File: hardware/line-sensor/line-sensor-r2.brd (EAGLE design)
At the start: 112 x 60 mm, 107 parts, among them IC1 GP2S60, IC10 GP2S60, IC11 GP2S60, IC12 GP2S60, IC13 GP2S60, IC14 GP2S60, IC15 GP2S60, IC16 GP2S60, IC17 GP2S60, IC18 GP2S60, IC19 GP2S60, IC2 GP2S60, IC20 GP2S60, IC21 GP2S60, IC22 GP2S60, IC23 GP2S60, IC24 STM32L151VE, IC25 GP2S60, IC26 GP2S60, IC27 ADR366BUJZ, IC28 TI-TPS62170, IC29 TI-LM5165YDRCR, IC3 GP2S60, IC30 ADP124ARHZ-3.3-R7CT-ND, IC4 GP2S60, IC5 GP2S60, IC6 GP2S60, IC7 GP2S60, IC8 GP2S60, IC9 GP2S60

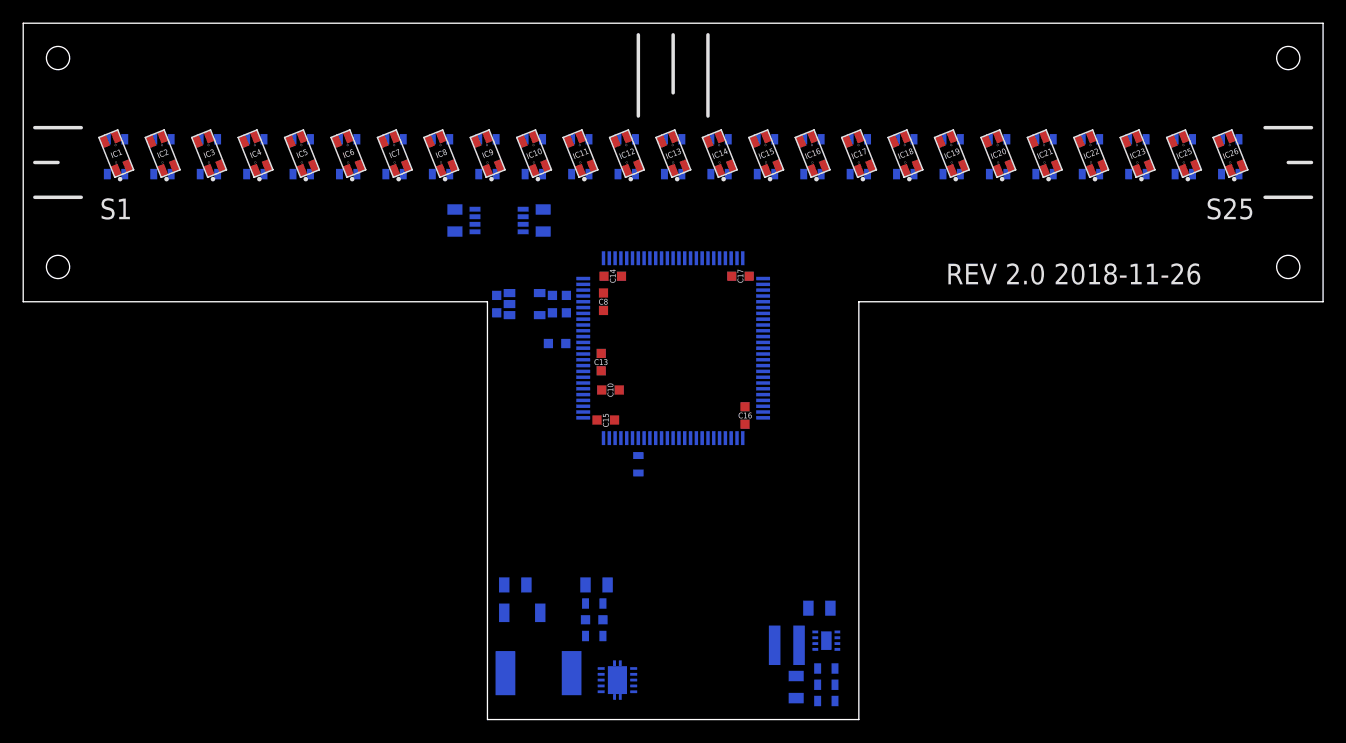
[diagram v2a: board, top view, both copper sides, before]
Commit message: - added line sensor power layout and mcu pin usage configuration
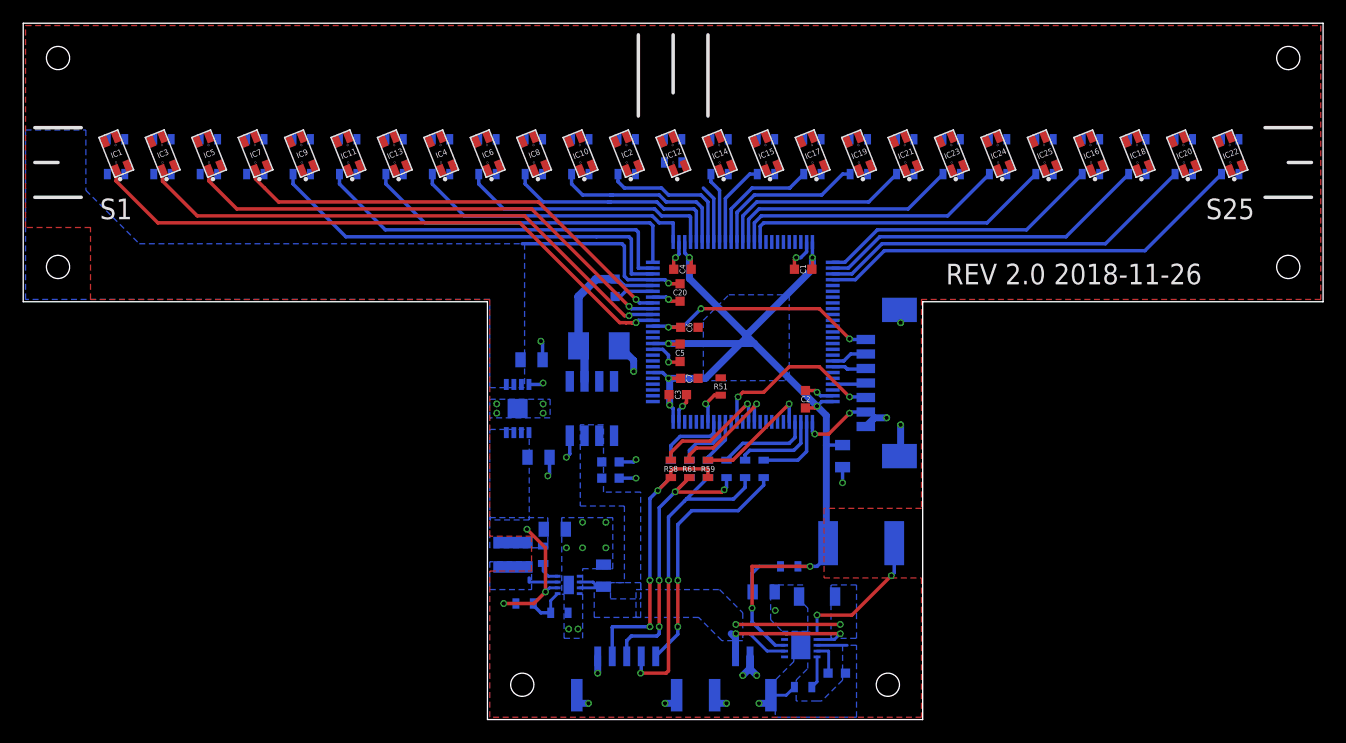
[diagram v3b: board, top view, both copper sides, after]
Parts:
- added C20: 0.1u 10V X7R, capacitors:CAPACITOR-0603
- added J1: MOLEX-502382-02XX, connectors:MOLEX-502382-02XX
- added J2: MOLEX-502382-05XX, connectors:MOLEX-502382-05XX
- added J3: MOLEX-53261-0771, connectors:MOLEX-53261-0771
- added R57, R58, R59, R60, R61, R62, R63, R64, R65: 0, resistors:RESISTOR-0603
- C1: value 0.1u 10V -> 0.1u
- C10: value 0.1u -> 33n 10V X7R
- C11: value 33n 10V X7R -> 22u 10V X7S; device capacitors:CAPACITOR-0603 -> capacitors:CAPACITOR-0805
- C13: value 0.1u -> 22u 10V X7R; device capacitors:CAPACITOR-0603 -> capacitors:CAPACITOR-0805
- C14: value 0.1u -> 10u 50V
- C15, C18: value 0.1u -> 1u 10V X7R; device capacitors:CAPACITOR-0603 -> capacitors:CAPACITOR-0805
- C16: value 0.1u -> 0.1u 50V
- C17: value 0.1u -> 1u 10V Tant; device capacitors:CAPACITOR-0603 -> capacitors:CAPACITOR_POLARIZED-1411-(3528-MET)
- C19: value 22u 10V X7R -> 0.1u 10V X7R; device capacitors:CAPACITOR-0805 -> capacitors:CAPACITOR-0603
- C2: value 0.1u 50V -> 0.1u
- C3, C4: value 1u 10V X7R -> 0.1u; device capacitors:CAPACITOR-0805 -> capacitors:CAPACITOR-0603
- C5: value 1u -> 0.1u
- C6: value 1u 50V X7R -> 0.1u; device capacitors:CAPACITOR-1206 -> capacitors:CAPACITOR-0603
- C7: value 22u 10V X7S -> 0.1u; device capacitors:CAPACITOR-0805 -> capacitors:CAPACITOR-0603
- C8: value 0.1u 10V X7R -> 10u 50V X7R; device capacitors:CAPACITOR-0603 -> capacitors:CAPACITOR-0805
- C9: value 10u 50V X7R -> 1u 50V X7R; device capacitors:CAPACITOR-0805 -> capacitors:CAPACITOR-1206
- IC24: value STM32L151VE -> GP2S60; device mcu:LQFP100_14X14 -> sensors:GP2S60
- IC26: value GP2S60 -> STM32L151VE; device sensors:GP2S60 -> mcu:LQFP100_14X14
- IC27: value ADR366BUJZ -> TI-LM5165YDRCR; device voltage-source:TSOT-25 -> voltage-source:VSON-10-0.5MM
- IC29: value TI-LM5165YDRCR -> AD-REF196GSZ; device voltage-source:VSON-10-0.5MM -> voltage-source:SOIC-8
- IC30: value ADP124ARHZ-3.3-R7CT-ND -> AD-ADP124ARHZ; device voltage-source:MSOP-8 -> voltage-source:MSOP-8-EP
- R10, R14, R18, R2, R22, R26, R30, R34, R38, R42, R6: value 220k -> 1k
- R11, R15, R19, R23, R27, R3, R31, R35, R39, R43, R7: value 1k -> 220k
- R51: value 121k 1% -> 100k
- R52: value 100k 1% -> 121k 1%
- R53: value 0.5 1% -> 100k 1%
- R54: value 100k -> 0.5 1%
- moved IC26 44.5 mm to (86.0, 49.4), flipped to the bottom, turned to 90 degrees
- moved R2 44.1 mm to (76.0, 66.0)
- moved IC2 40.0 mm to (76.0, 64.0)
- moved R4 40.0 mm to (76.0, 63.0)
- moved IC27 37.8 mm to (91.0, 22.4), turned to 0 degrees
- moved C19 37.8 mm to (75.0, 53.2)
- moved IC24 32.2 mm to (108.0, 64.0), flipped to the top, turned to 111.8 degrees
- moved C10 31.2 mm to (94.1, 20.0), flipped to the bottom, turned to 180 degrees
- moved L2 30.0 mm to (96.2, 31.2), turned to 0 degrees
- moved C6 28.5 mm to (81.4, 49.8), flipped to the top
- moved R27 28.2 mm to (56.0, 63.0)
- moved R30 28.2 mm to (116.0, 66.0)
- moved C2 27.8 mm to (91.4, 43.6), flipped to the top, turned to 90 degrees
- moved R55 26.9 mm to (67.2, 26.0)
- moved L1 24.9 mm to (66.2, 30.2), turned to 90 degrees
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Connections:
- net N$26 renamed IC28_SW
- removed net AGND: C1.2, C3.2, C5.2, C8.2, IC1.2, IC1.3, IC10.2, IC10.3, IC11.2, IC11.3, IC12.2, IC12.3, IC13.2, IC13.3, IC14.2, IC14.3, IC15.2, IC15.3, IC16.2, IC16.3, IC17.2, IC17.3, IC18.2, IC18.3, IC19.2, IC19.3, IC2.2, IC2.3, IC20.2, IC20.3, IC21.2, IC21.3, IC22.2, IC22.3, IC23.2, IC23.3, IC24.19, IC24.20, IC25.2, IC25.3, IC26.2, IC26.3, IC3.2, IC3.3, IC30.4, IC4.2, IC4.3, IC5.2, IC5.3, IC6.2, IC6.3, IC7.2, IC7.3, IC8.2, IC8.3, IC9.2, IC9.3
- removed net DGND: C10.2, C11.2, C12.2, C13.2, C14.2, C15.2, C16.2, C17.2, C18.2, C7.2, IC24.10, IC24.27, IC24.49, IC24.74, IC24.99, IC29.10, IC29.11, IC29.3, R54.P$2
- removed net N$1 (its old number): IC2.4, R3.P$1
- removed net N$16 (its old number): IC16.4, R31.P$1
- removed net N$18 (its old number): IC18.4, R35.P$1
- removed net N$30: IC29.5, R51.P$1
- removed net N$32: C7.1, R53.P$2
- removed net N$4 (its old number): IC4.4, R7.P$1
- removed net N$6 (its old number): IC6.4, R11.P$1
- removed net V3.5: C19.1, C4.1, IC28.6, IC30.5, IC30.7, IC30.8, L1.2, R52.P$2, R55.P$2
- new net I2C1_SCL: IC26.92, R60.P$1
- new net I2C1_SDA: IC26.93, R57.P$1
- new net I2C1_SMBA: IC26.91, R64.P$2
- new net IC27_SW: IC27.1, L2.1
- new net N$11: IC10.4, R18.P$1
- new net N$13: IC12.4, R22.P$1
- new net N$21: IC25.4, R49.P$1
- new net N$23: IC18.4, R34.P$1
- new net N$26: J2.2, R57.P$2, R58.P$2, R59.P$2
- new net N$33: IC27.5, R52.P$1
- new net N$34: C10.1, IC27.4
- new net N$36: C11.1, R54.P$2
- new net N$38: IC28.8, R53.P$1
- new net N$9: IC6.4, R10.P$1
- new net SPI3_MISO: IC26.79, R62.P$1
- new net SPI3_MOSI: IC26.80, R59.P$1
- new net SPI3_NSS: IC26.77, R65.P$2
- new net SPI3_SCK: IC26.78, R63.P$2
- new net STLINK_SWO: IC26.89, J3.5
- new net STLINK_TCK: IC26.76, J3.6
- new net STLINK_TMS: IC26.72, J3.4
- new net STLINK_USART1_RX: IC26.69, J3.3
- new net STLINK_USART1_TX: IC26.68, J3.2
- new net USART2_RX: IC26.87, R58.P$1
- new net USART2_TX: IC26.86, R61.P$1
- new net VDDA3.5: C13.1, C15.1, IC28.6, IC30.5, IC30.7, IC30.8, L1.2, R53.P$2, R55.P$2
- net !RST: now also C6.1, IC26.14, J3.1; no longer C18.1, IC24.14
- net 3V1: now also R38.P$2, R40.P$2; no longer R47.P$2, R48.P$2
- net 3V2: now also R42.P$2, R44.P$2; no longer R49.P$2, R50.P$2
- net 3V3: now also R47.P$2, R48.P$2, R49.P$2, R50.P$2; no longer R38.P$2, R40.P$2, R42.P$2, R44.P$2
- net BOOT0: now also IC26.94, R51.P$1; no longer IC24.94, R54.P$1
- net GND: now also C1.2, C10.2, C11.2, C12.2, C13.2, C14.2, C15.2, C16.2, C17.NEG, C18.2, C20.2, C3.2, C5.2, C6.2, C7.2, C8.2, C9.P$2, IC1.2, IC1.3, IC10.2, IC10.3, IC11.2, IC11.3, IC12.2, IC12.3, IC13.2, IC13.3, IC14.2, IC14.3, IC15.2, IC15.3, IC16.2, IC16.3, IC17.2, IC17.3, IC18.2, IC18.3, IC19.2, IC19.3, IC2.2, IC2.3, IC20.2, IC20.3, IC21.2, IC21.3, IC22.2, IC22.3, IC23.2, IC23.3, IC24.2, IC24.3, IC25.2, IC25.3, IC26.10, IC26.19, IC26.20, IC26.27, IC26.49, IC26.74, IC26.99, IC27.10, IC27.11, IC27.3, IC29.4, IC3.2, IC3.3, IC30.4, IC30.PAD, IC4.2, IC4.3, IC5.2, IC5.3, IC6.2, IC6.3, IC7.2, IC7.3, IC8.2, IC8.3, IC9.2, IC9.3, J1.2, J1.G1, J1.G2, J2.1, J2.G1, J2.G2, J3.7, J3.G1, J3.G2, R52.P$2; no longer C6.P$2, C9.2, IC27.2
- net N$10: now also IC8.4, R14.P$1; no longer IC10.4, R19.P$1
- net N$12: now also IC2.4, R2.P$1; no longer IC12.4, R23.P$1
- net N$14: now also R26.P$1; no longer R27.P$1
- net N$20: now also IC24.4, R47.P$1; no longer IC20.4, R39.P$1
- net N$22: now also IC16.4, R30.P$1; no longer IC22.4, R43.P$1
- net N$24: now also IC20.4, R38.P$1; no longer IC25.4, R47.P$1
- net N$25: now also IC22.4, R42.P$1; no longer IC26.4, R49.P$1
- net N$27: now also J2.3, R60.P$2, R61.P$2, R62.P$2; no longer IC28.8, R52.P$1
- net N$28: now also J2.4, R63.P$1, R64.P$1; no longer C11.1, IC29.4
- net N$29: now also J2.5, R65.P$1; no longer IC29.1, L2.1
- net N$8: now also IC4.4, R6.P$1; no longer IC8.4, R15.P$1
- net SENSOR_1: now also IC26.15, R3.P$1; no longer IC24.15, R2.P$1
- net SENSOR_10: now also IC26.30, IC8.1, R16.P$1; no longer IC10.1, IC24.30, R20.P$1
- net SENSOR_11: now also IC10.1, IC26.31, R20.P$1; no longer IC11.1, IC24.31, R22.P$1
- net SENSOR_12: now also IC2.1, IC26.32, R4.P$1; no longer IC12.1, IC24.32, R24.P$1
- net SENSOR_13: now also IC12.1, IC26.33, R24.P$1; no longer IC13.1, IC24.33, R26.P$1
- net SENSOR_14: now also IC26.34; no longer IC24.34
- net SENSOR_15: now also IC26.35, R31.P$1; no longer IC24.35, R30.P$1
- net SENSOR_16: now also IC17.1, IC26.36, R35.P$1; no longer IC16.1, IC24.36, R32.P$1
- net SENSOR_17: now also IC19.1, IC26.37, R39.P$1; no longer IC17.1, IC24.37, R34.P$1
- net SENSOR_18: now also IC21.1, IC26.38, R43.P$1; no longer IC18.1, IC24.38, R36.P$1
- net SENSOR_19: now also IC23.1, IC26.39, R46.P$1; no longer IC19.1, IC24.39, R38.P$1
- net SENSOR_2: now also IC26.16, IC3.1, R7.P$1; no longer IC2.1, IC24.16, R4.P$1
- net SENSOR_20: now also IC24.1, IC26.40, R48.P$1; no longer IC20.1, IC24.40, R40.P$1
- net SENSOR_21: now also IC25.1, IC26.41, R50.P$1; no longer IC21.1, IC24.41, R42.P$1
- net SENSOR_22: now also IC16.1, IC26.51, R32.P$1; no longer IC22.1, IC24.51, R44.P$1
- net SENSOR_23: now also IC18.1, IC26.52, R36.P$1; no longer IC23.1, IC24.52, R46.P$1
- net SENSOR_24: now also IC20.1, IC26.53, R40.P$1; no longer IC24.53, IC25.1, R48.P$1
- net SENSOR_25: now also IC22.1, IC26.54, R44.P$1; no longer IC24.54, IC26.1, R50.P$1
- net SENSOR_3: now also IC26.17, IC5.1, R11.P$1; no longer IC24.17, IC3.1, R6.P$1
- net SENSOR_4: now also IC26.18, IC7.1, R15.P$1; no longer IC24.18, IC4.1, R8.P$1
- net SENSOR_5: now also IC26.23, IC9.1, R19.P$1; no longer IC24.23, IC5.1, R10.P$1
- net SENSOR_6: now also IC11.1, IC26.24, R23.P$1; no longer IC24.24, IC6.1, R12.P$1
- net SENSOR_7: now also IC13.1, IC26.25, R27.P$1; no longer IC24.25, IC7.1, R14.P$1
- net SENSOR_8: now also IC26.26, IC4.1, R8.P$1; no longer IC24.26, IC8.1, R16.P$1
- net SENSOR_9: now also IC26.29, IC6.1, R12.P$1; no longer IC24.29, IC9.1, R18.P$1
- net VBAT: now also C14.1, C16.1, C8.1, C9.P$1, IC27.2, IC27.7, IC29.3, J1.1; no longer C2.1, C6.P$1, C9.1, IC27.3, IC29.7
- net VDD: now also C1.1, C2.1, C3.1, C4.1, C5.1, C7.1, IC26.100, IC26.11, IC26.28, IC26.50, IC26.6, IC26.75, IC27.8, R54.P$1; no longer C10.1, C13.1, C14.1, C15.1, C16.1, C17.1, IC24.100, IC24.11, IC24.28, IC24.50, IC24.6, IC24.75, IC29.8, R53.P$1
- net VDDA: now also C18.1, C20.1, IC26.22; no longer C3.1, C8.1, IC24.22
- net VREF3.3: now also C17.POS, C19.1, IC26.21, IC29.6; no longer C1.1, C5.1, IC24.21, IC27.4
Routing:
- net VDD: track 0.00 -> 90.6 mm, vias 0 -> 8
- net GND: track 0.00 -> 59.0 mm, vias 0 -> 36
- net SENSOR_1: track 0.00 -> 52.3 mm, vias 0 -> 1
- net SENSOR_2: track 0.00 -> 48.0 mm, vias 0 -> 1
- net SENSOR_3: track 0.00 -> 43.7 mm, vias 0 -> 1
- net SENSOR_4: track 0.00 -> 39.4 mm, vias 0 -> 1
- net SENSOR_25: track 0.00 -> 37.3 mm
- net SENSOR_5: track 0.00 -> 36.8 mm
- net SENSOR_24: track 0.00 -> 33.1 mm
- net SENSOR_6: track 0.00 -> 32.7 mm
- net VBAT: track 0.00 -> 31.1 mm, vias 0 -> 4
- net SENSOR_23: track 0.00 -> 28.9 mm
- net SENSOR_7: track 0.00 -> 28.5 mm
- net N$28: track 0.00 -> 28.3 mm, vias 0 -> 2
- net SENSOR_21: track 0.00 -> 27.0 mm
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- added copper zone on layer 1, net GND
- added copper zone on layer 16, net GND
- added copper zone on layer 16, net IC28_SW
- added copper zone on layer 16, net VBAT
- added copper zone on layer 16, net VDD
- added copper zone on layer 16, net VDDA
- added copper zone on layer 16, net VDDA3.5
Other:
- outline, holes or cut-outs redrawn

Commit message: - finished line sensor with linear regulator and voltage reference
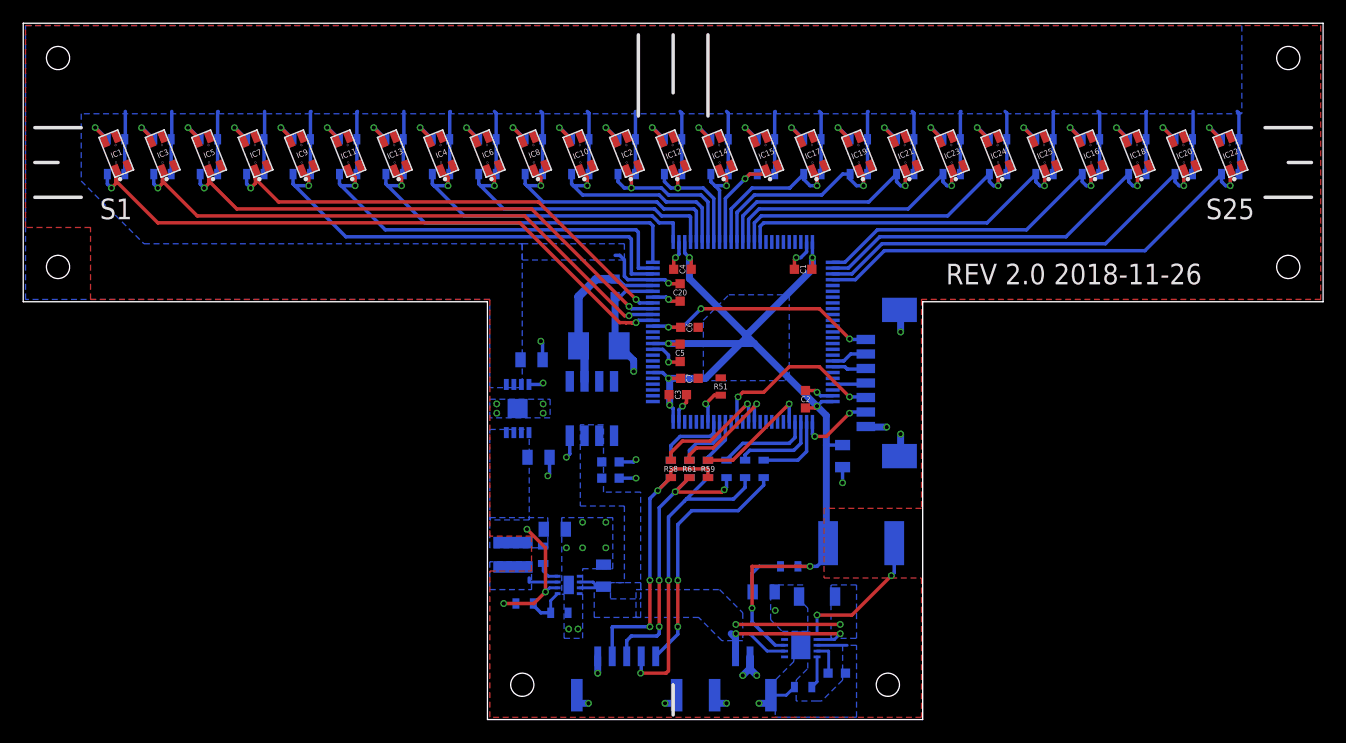
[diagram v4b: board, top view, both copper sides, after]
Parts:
- moved R24 1.00 mm to (80.0, 63.0)
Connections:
- removed net 3V1: R38.P$2, R40.P$2
- removed net 3V2: R42.P$2, R44.P$2
- removed net 3V3: R1.P$2, R10.P$2, R11.P$2, R12.P$2, R13.P$2, R14.P$2, R15.P$2, R16.P$2, R17.P$2, R18.P$2, R19.P$2, R2.P$2, R20.P$2, R21.P$2, R22.P$2, R23.P$2, R24.P$2, R25.P$2, R26.P$2, R27.P$2, R28.P$2, R29.P$2, R3.P$2, R30.P$2, R31.P$2, R32.P$2, R33.P$2, R34.P$2, R35.P$2, R36.P$2, R37.P$2, R39.P$2, R4.P$2, R41.P$2, R43.P$2, R45.P$2, R46.P$2, R47.P$2, R48.P$2, R49.P$2, R5.P$2, R50.P$2, R6.P$2, R7.P$2, R8.P$2, R9.P$2
- net VDDA: now also R1.P$2, R10.P$2, R11.P$2, R12.P$2, R13.P$2, R14.P$2, R15.P$2, R16.P$2, R17.P$2, R18.P$2, R19.P$2, R2.P$2, R20.P$2, R21.P$2, R22.P$2, R23.P$2, R24.P$2, R25.P$2, R26.P$2, R27.P$2, R28.P$2, R29.P$2, R3.P$2, R30.P$2, R31.P$2, R32.P$2, R33.P$2, R34.P$2, R35.P$2, R36.P$2, R37.P$2, R38.P$2, R39.P$2, R4.P$2, R40.P$2, R41.P$2, R42.P$2, R43.P$2, R44.P$2, R45.P$2, R46.P$2, R47.P$2, R48.P$2, R49.P$2, R5.P$2, R50.P$2, R6.P$2, R7.P$2, R8.P$2, R9.P$2
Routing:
- net VDDA: track 16.6 -> 143.4 mm
- net SENSOR_13: track 5.02 -> 10.9 mm, vias 0 -> 1
- net GND: track 59.0 -> 63.1 mm
- net SENSOR_17: track 13.7 -> 17.0 mm, vias 0 -> 1
- net SENSOR_16: track 10.3 -> 13.6 mm, vias 0 -> 1
- net SENSOR_4: track 39.4 -> 42.4 mm, vias 1 -> 2
- net SENSOR_3: track 43.7 -> 46.7 mm, vias 1 -> 2
- net SENSOR_1: track 52.3 -> 55.3 mm, vias 1 -> 2
- net N$2: track 0.00 -> 2.99 mm, vias 0 -> 1
- net N$25: track 0.00 -> 2.99 mm, vias 0 -> 1
- net N$24: track 0.00 -> 2.99 mm, vias 0 -> 1
- net N$23: track 0.00 -> 2.99 mm, vias 0 -> 1
- net N$22: track 0.00 -> 2.99 mm, vias 0 -> 1
- net N$21: track 0.00 -> 2.99 mm, vias 0 -> 1
- net N$20: track 0.00 -> 2.99 mm, vias 0 -> 1
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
